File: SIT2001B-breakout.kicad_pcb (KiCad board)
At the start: 2 copper layers, 10.5 x 7.6 mm, 8 parts, among them J1 Conn_01x03, U1 SiT2001B-MEMS-Clock-Generator, U2 NJM2866F33

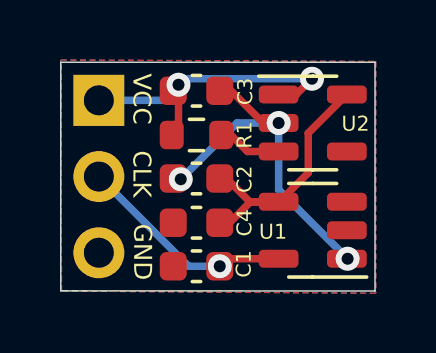
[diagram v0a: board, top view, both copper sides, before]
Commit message: Correct warning and error of drc
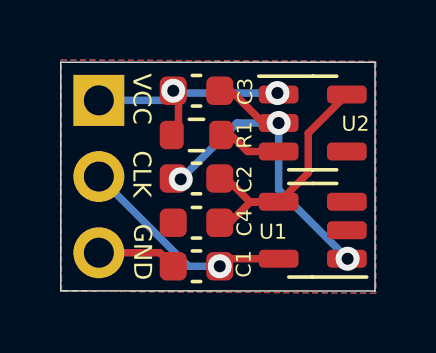
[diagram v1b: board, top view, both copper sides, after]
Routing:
- net GND: track 11.8 -> 14.5 mm
- net VCC: track 10.3 -> 8.00 mm
